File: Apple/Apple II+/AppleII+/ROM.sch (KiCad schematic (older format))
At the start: 8 parts

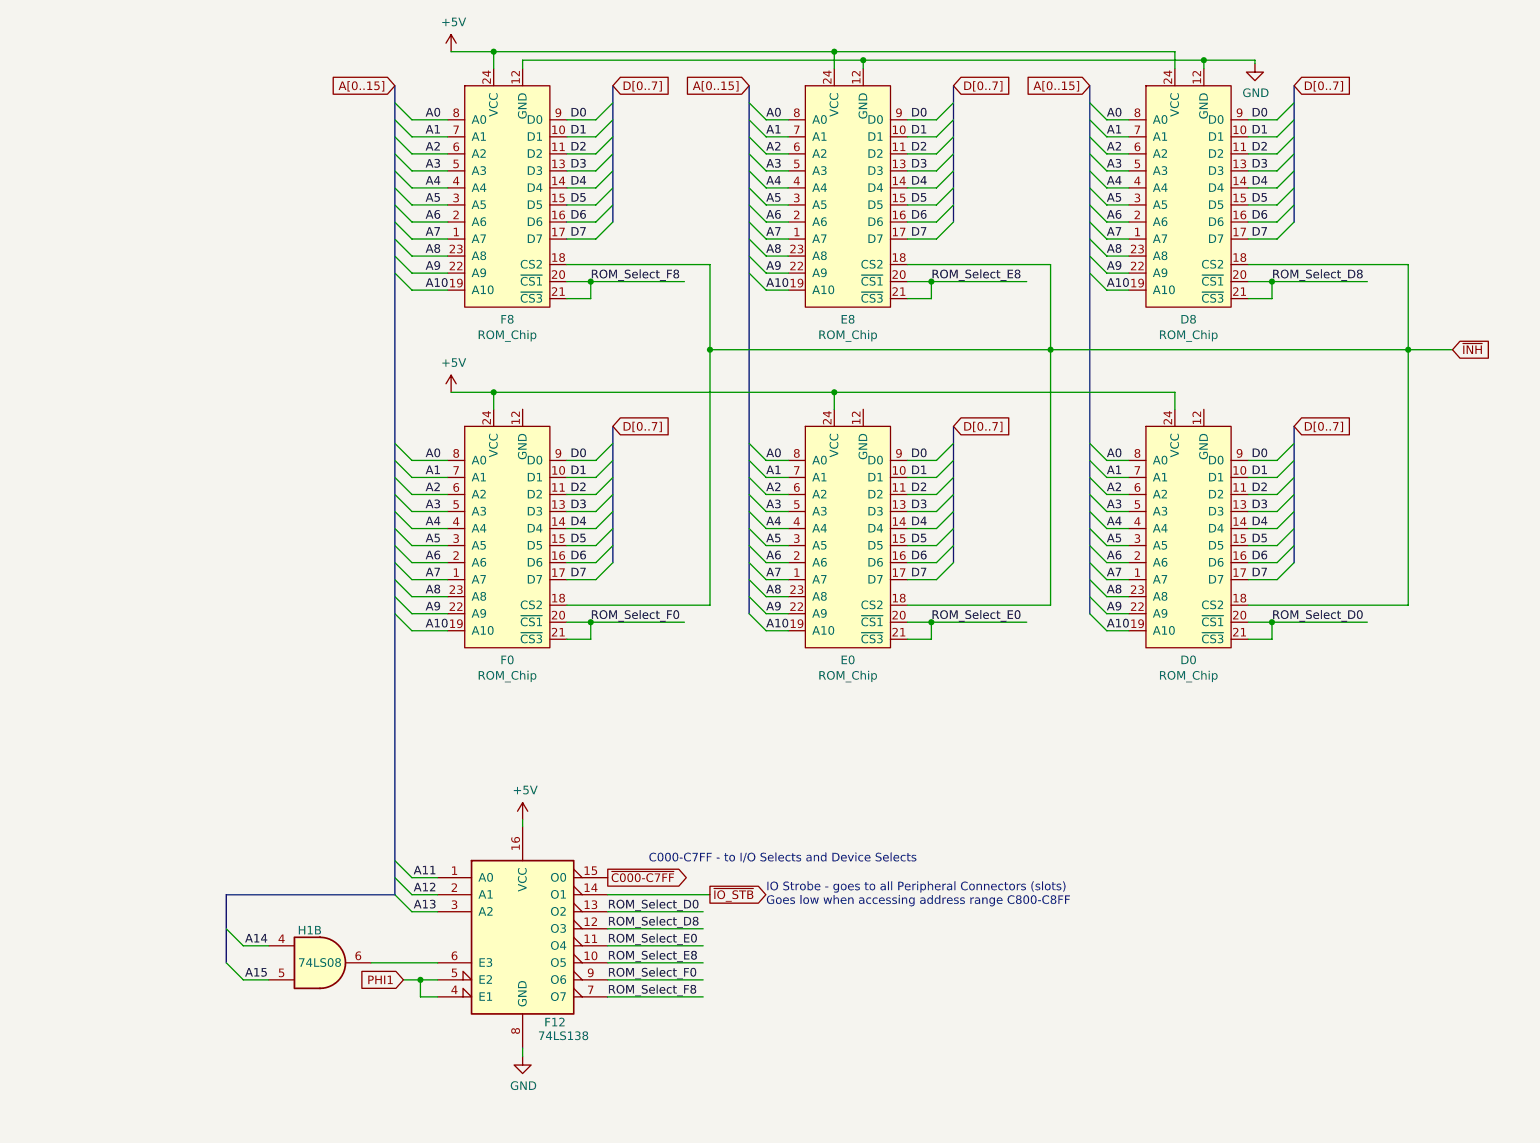
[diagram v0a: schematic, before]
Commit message: added RAM sheet, updated address decode sheet
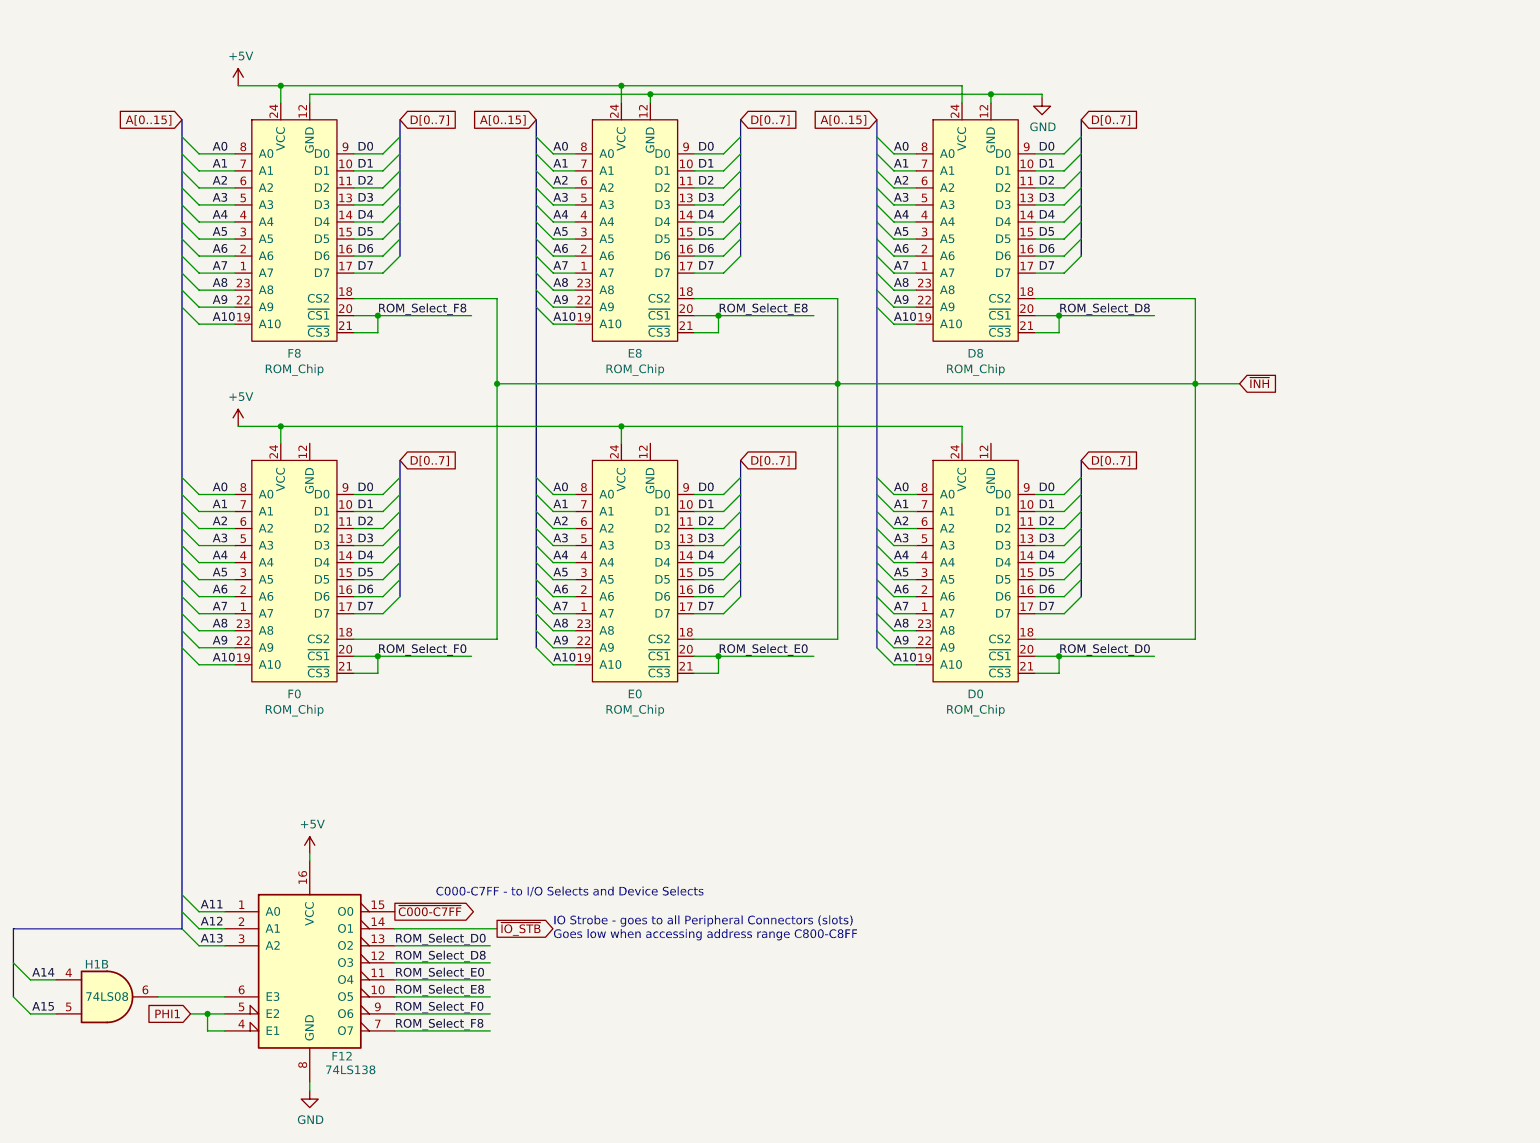
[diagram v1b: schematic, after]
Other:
- moved on the sheet: D0, D8, E0, E8, F0, F12, F8, H1B

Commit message: More updating in RAM decoding sheet
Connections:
- wire segments 191 -> 197
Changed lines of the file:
@@
 $Descr A4 11693 8268
 encoding utf-8
-Sheet 3 8
+Sheet 3 9
 Title "Apple II+ Schematic"
 Date ""
-Rev ""
+Rev "0"
 Comp ""
 Comment1 "Captured from the Apple II Reference Manual (1979)"
@@
 P 8050 1220
 F 0 "#PWR?" H 8050 970 50  0001 C CNN
-F 1 "GND" H 8055 1047 50  0000 C CNN
+F 1 "GND" H 8130 1210 50  0000 C CNN
 F 2 "" H 8050 1220 50  0001 C CNN
 F 3 "" H 8050 1220 50  0001 C CNN
@@
 U 1 1 6035532D
 P 3750 6300
-F 0 "F12" H 3940 5750 50  0000 C CNN
-F 1 "74LS138" H 3990 5670 50  0000 C CNN
+F 0 "F12" H 3990 6820 50  0000 C CNN
+F 1 "74LS138" H 3920 6740 50  0000 C CNN
 F 2 "" H 3750 6300 50  0001 C CNN
 F 3 "http://www.ti.com/lit/gpn/sn74LS138" H 3750 6300 50  0001 C CNN
@@
 Wire Wire Line
 	4250 6700 4810 6700
+$Comp
+L power:GND #PWR?
+U 1 1 602051A9
+P 8000 3200
+F 0 "#PWR?" H 8000 2950 50  0001 C CNN
+F 1 "GND" H 8080 3190 50  0000 C CNN
+F 2 "" H 8000 3200 50  0001 C CNN
+F 3 "" H 8000 3200 50  0001 C CNN
+	1    8000 3200
+	1    0    0    -1
+$EndComp
+Wire Wire Line
+	7750 3200 5750 3200
+Wire Wire Line
+	3750 3200 3750 3250
+Wire Wire Line
+	7750 3200 7750 3250
+Wire Wire Line
+	5750 3250 5750 3200
+Connection ~ 5750 3200
+Wire Wire Line
+	5750 3200 3750 3200
+Wire Wire Line
+	7750 3200 8000 3200
 Wire Bus Line
 	2010 6100 2010 6500
@@
 Wire Bus Line
 	7080 1350 7080 4450
+Connection ~ 7750 3200
 $EndSCHEMATC
